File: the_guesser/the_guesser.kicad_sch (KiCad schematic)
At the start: 24 parts, among them Q11 2N7002, U1 ESP32-S3FN8, U10 TPS61033DRLR, U2 W25Q128JVS, X002 ECS-3953M-400-AU-TR, X2 XRCGB40M000F1S2GR0

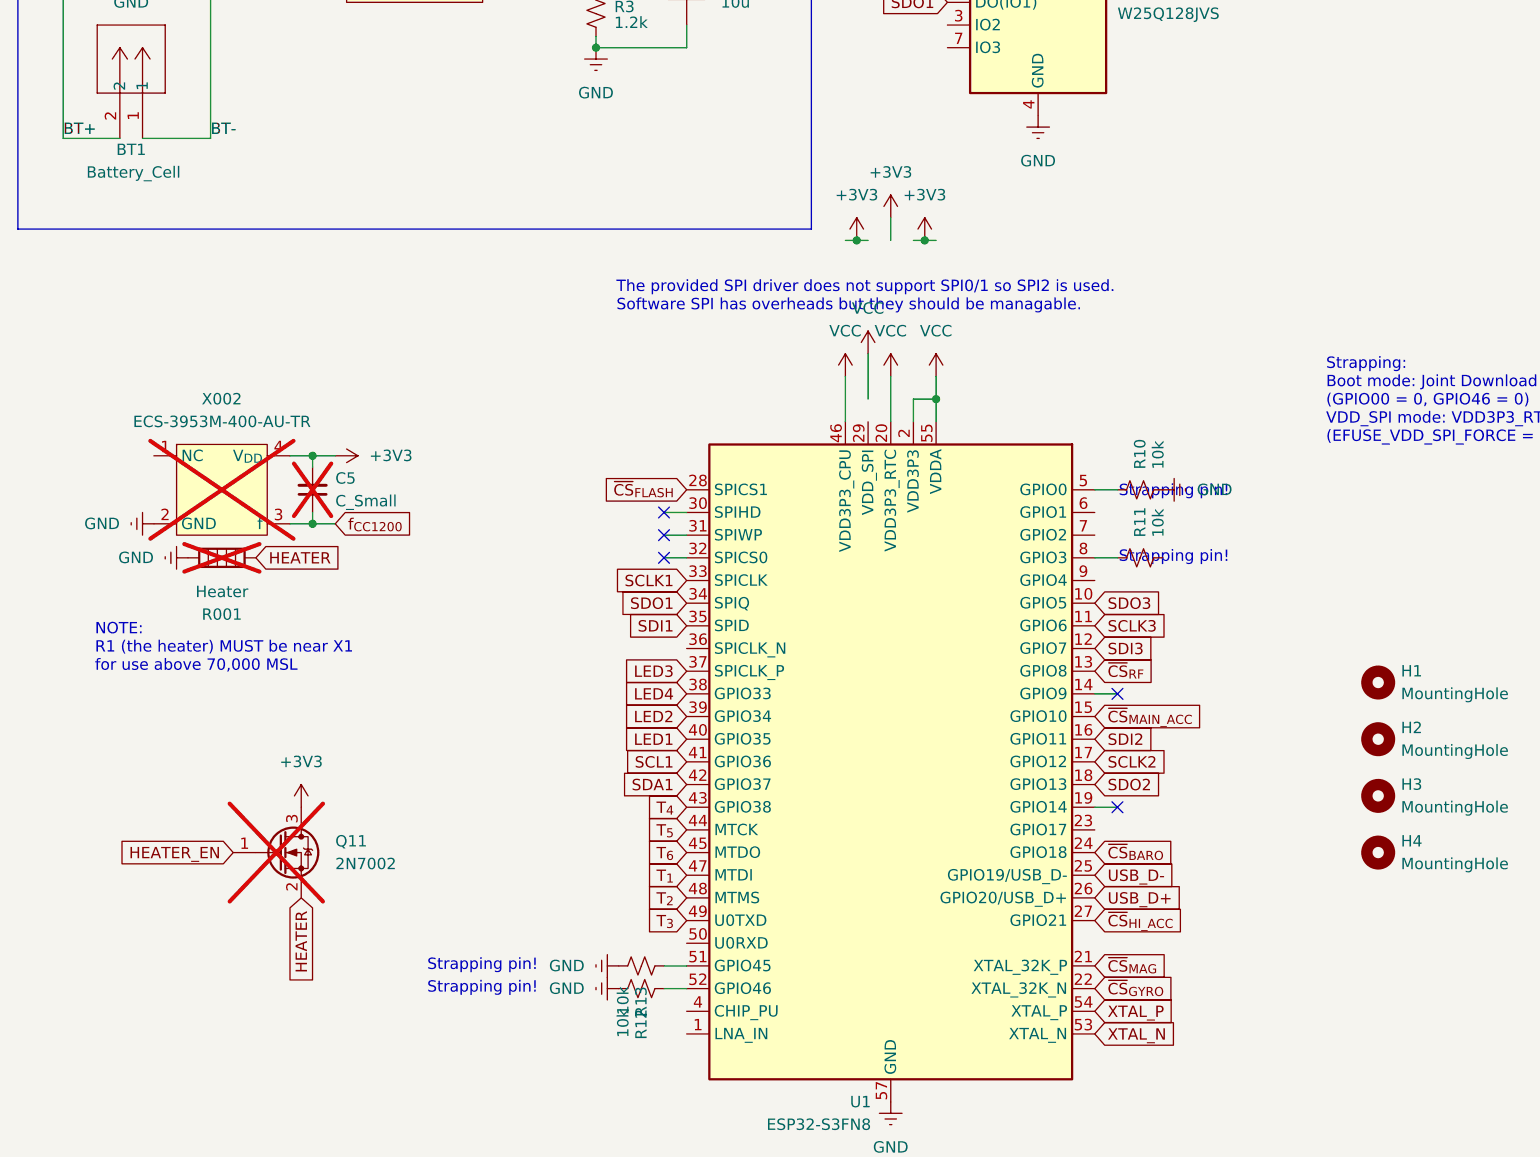
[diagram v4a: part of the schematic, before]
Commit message: Cleaned up Guesser schematic a bit
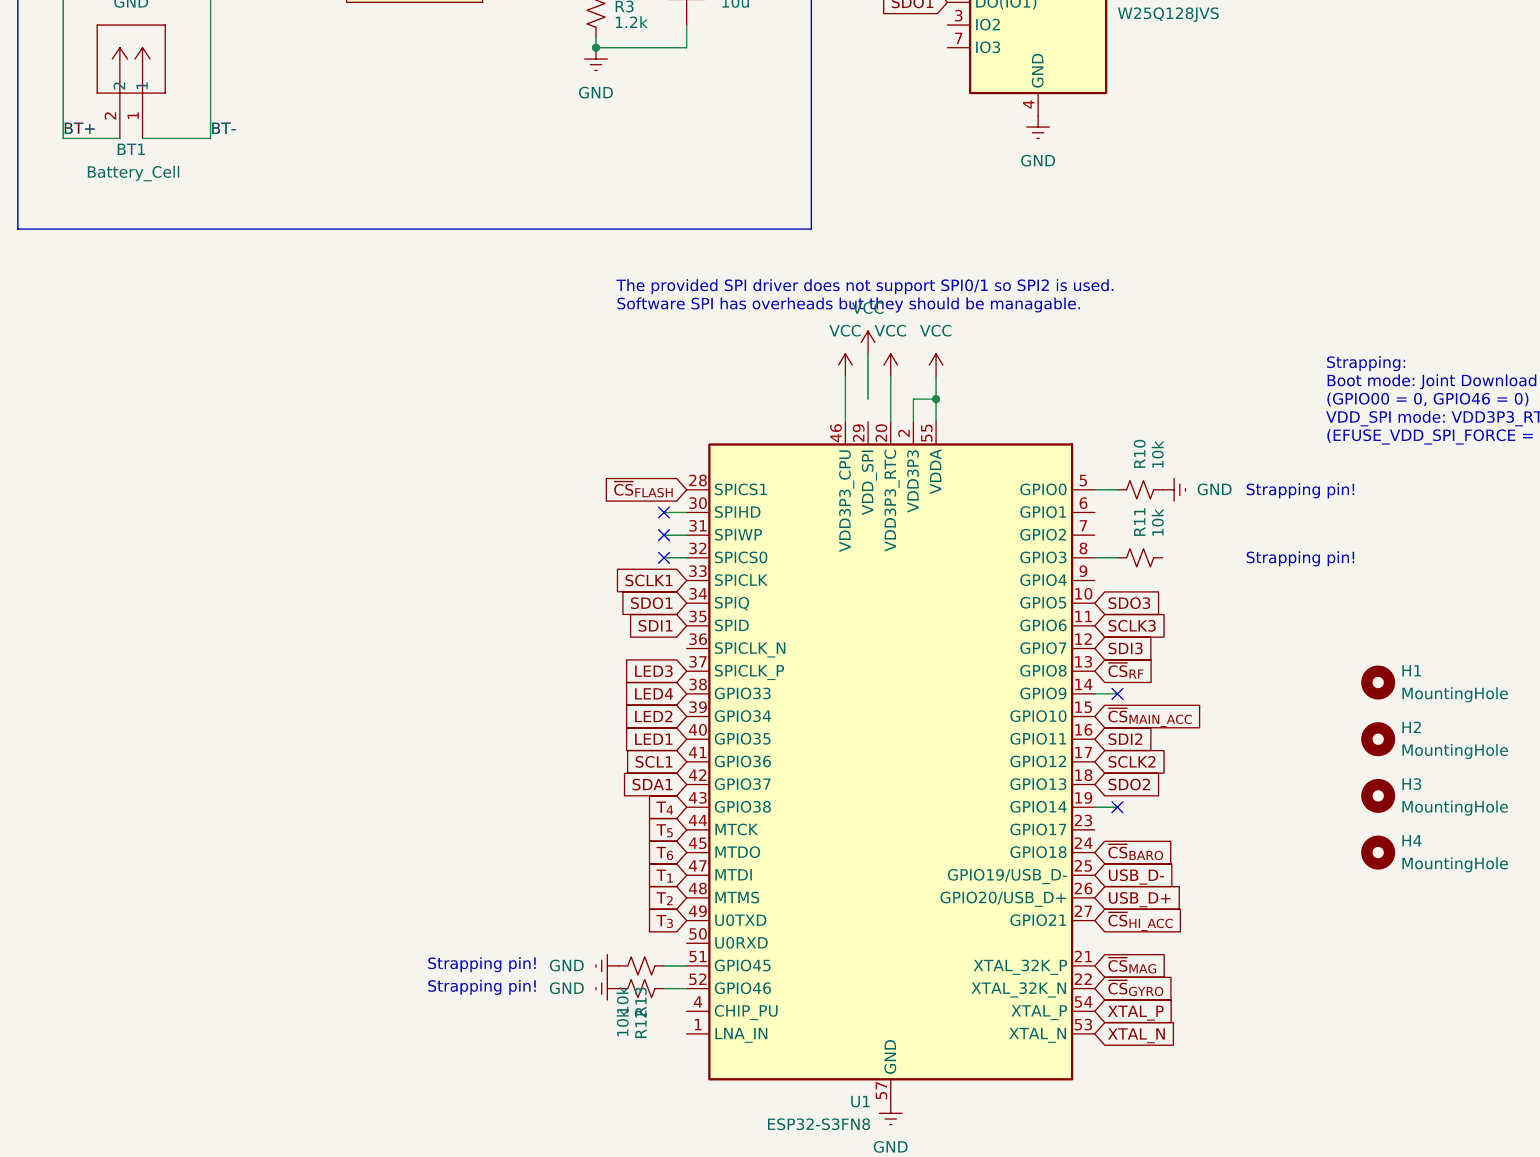
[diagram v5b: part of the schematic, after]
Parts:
- removed C5: C_Small, symbol Device:C_Small
- removed Q11: 2N7002, Package_TO_SOT_SMD:SOT-23, symbol Transistor_FET:2N7002
- removed R001: Heater, symbol Device:Heater
- removed X002: ECS-3953M-400-AU-TR, Crystal:Crystal_SMD_5032-4Pin_5.0x3.2mm, symbol locals:ECS-3953M-400-AU-TR
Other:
- note removed: "NOTE: R1 (the heater) MUST be near X1 for use above 70,000 MSL"

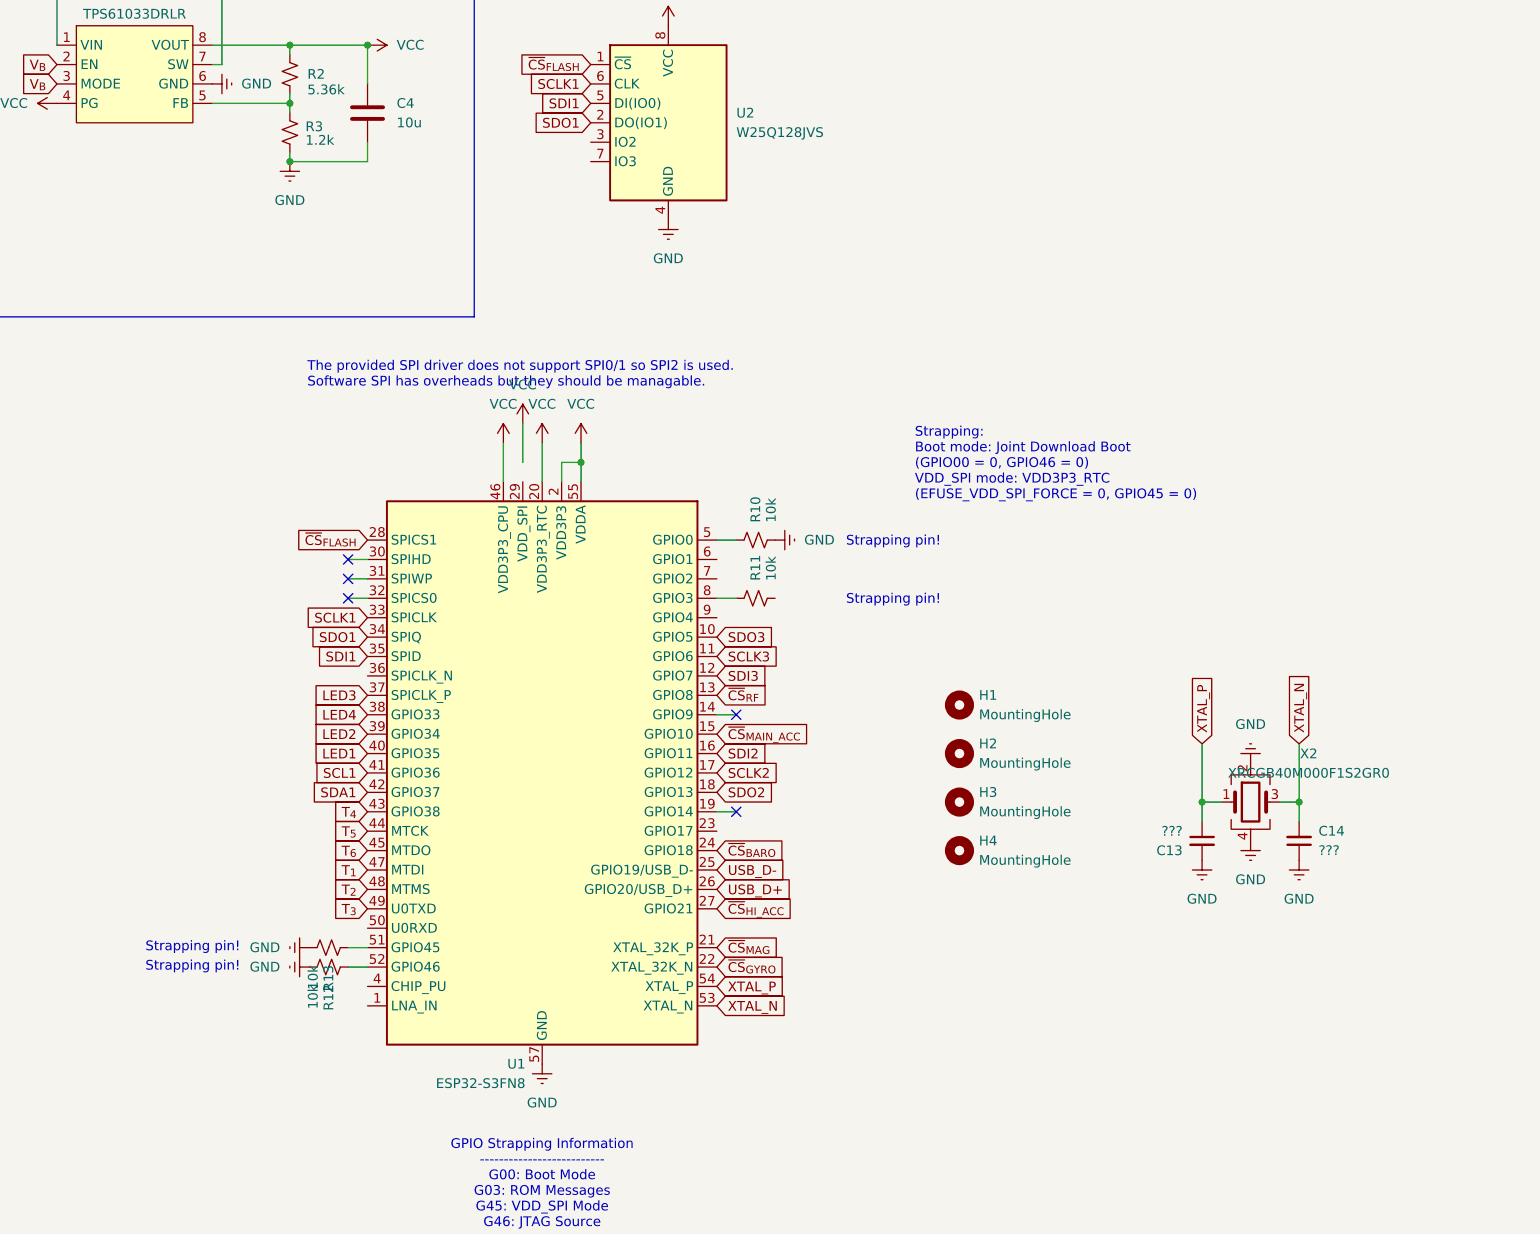
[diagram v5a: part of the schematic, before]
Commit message: Updated Guesser USB and GPS
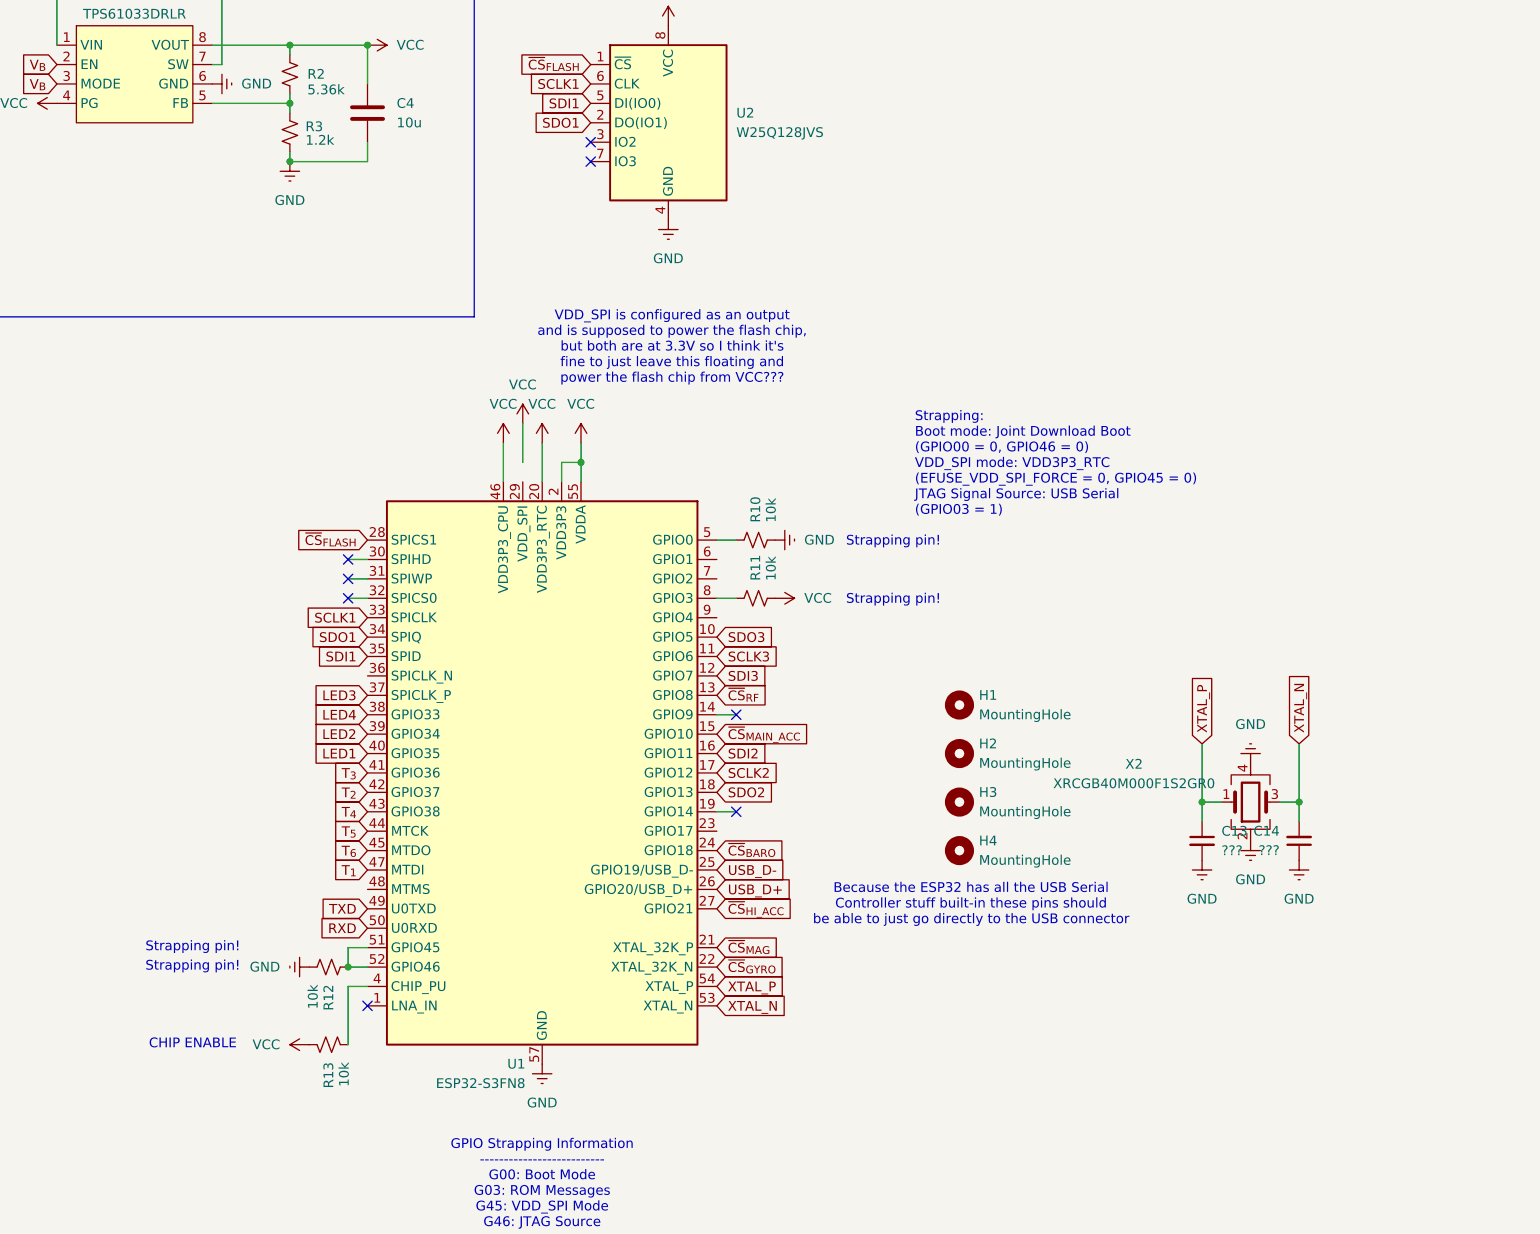
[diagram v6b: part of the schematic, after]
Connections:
- net SCL1 is gone; now on net T_{3}: U1.41 (GPIO36)
- net SDA1 is gone; now on net T_{2}: U1.42 (GPIO37)
- net GND: no longer R13.2
- net T_{2}: no longer U1.48 (MTMS)
- net T_{3}: no longer U1.49 (U0TXD)
- net VCC: now also R11.2, R13.1
- net at R12.1, U1.52 (GPIO46): now also U1.51 (GPIO45)
- net at U1.4 (CHIP_PU): now also R13.2
- net RXD: now reaches U1.50 (U0RXD)
- new net TXD: U1.49 (U0TXD)
- no-connect marks 5 -> 8
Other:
- note added: "Because the ESP32 has all the USB Serial Controller stuff built-in these pins should be able to just go directly to the USB connector"
- note added: "CHIP ENABLE"
- note added: "Strapping: Boot mode: Joint Download Boot (GPIO00 = 0, GPIO46 = 0) VDD_SPI mode: VDD3P3_RTC (EFUSE_VDD_SPI_FORCE = 0, GPIO45 = 0) JTAG Signal Source: USB Serial (GPIO03 = 1)"
- note added: "VDD_SPI is configured as an output and is supposed to power the flash chip, but both are at 3.3V so I think it's fine to just leave this floating and power the flash chip from VCC???"
- note removed: "Strapping: Boot mode: Joint Download Boot (GPIO00 = 0, GPIO46 = 0) VDD_SPI mode: VDD3P3_RTC (EFUSE_VDD_SPI_FORCE = 0, GPIO45 = 0)"
- note removed: "The provided SPI driver does not support SPI0/1 so SPI2 is used. Software SPI has overheads but they should be managable."
- moved on the sheet: C14
